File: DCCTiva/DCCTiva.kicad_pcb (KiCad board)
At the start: 2 copper layers, 50.8 x 34.3 mm, 11 parts, among them J1 TI_BOOSTER_40_J1, J2 TI_BOOSTER_40_J2, J3 TI_BOOSTER_40_J3, J4 TI_BOOSTER_40_J4, P1 Power and DCC, U1 LMD18200

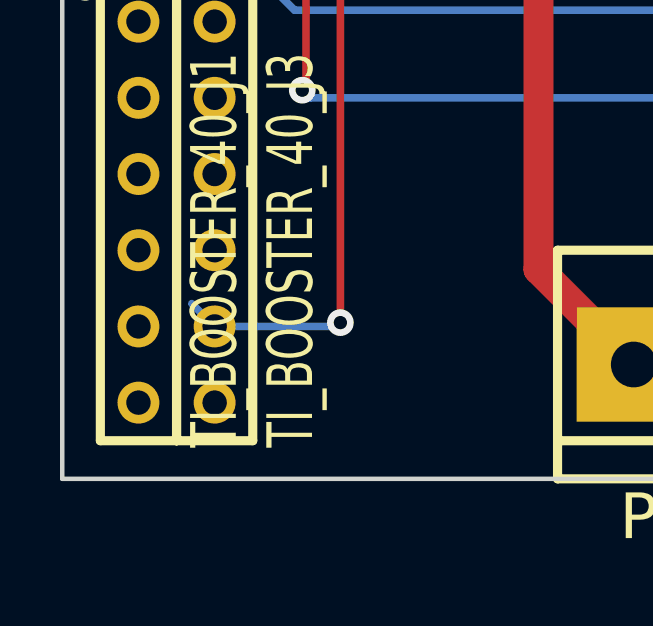
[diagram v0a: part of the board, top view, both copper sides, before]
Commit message: Add Current Sense line
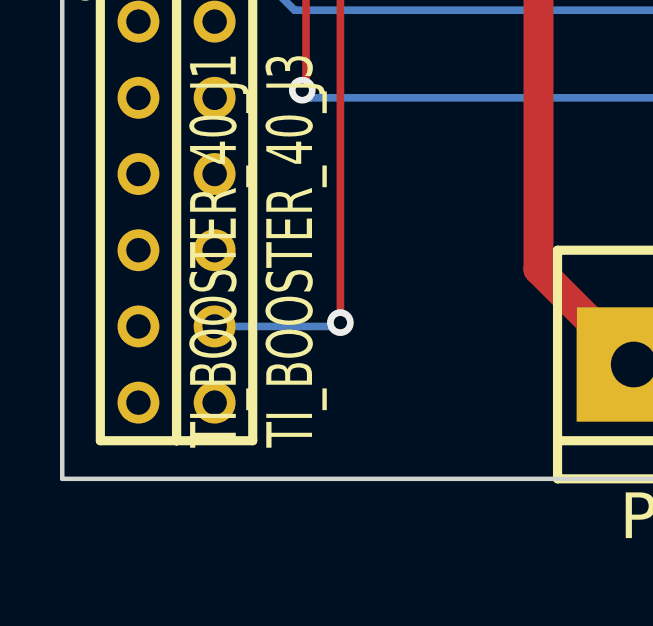
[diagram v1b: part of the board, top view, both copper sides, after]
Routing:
- net /Current Sense: track 48.1 -> 47.0 mm
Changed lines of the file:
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@@
     (thickness 1.6)
     (drawings 7)
-    (tracks 121)
+    (tracks 120)
     (zones 0)
     (modules 11)
@@
   (segment (start 192.532 129.54) (end 192.151 129.921) (width 0.254) (layer Front) (net 3))
   (via (at 192.532 129.54) (size 0.889) (layers Front Back) (net 3))
-  (segment (start 187.96 142.24) (end 187.198 141.478) (width 0.254) (layer Back) (net 3))
   (segment (start 200.66 129.54) (end 205.105 129.54) (width 0.254) (layer Back) (net 3))
   (segment (start 212.95 120.171) (end 212.95 118.59) (width 0.254) (layer Front) (net 3))

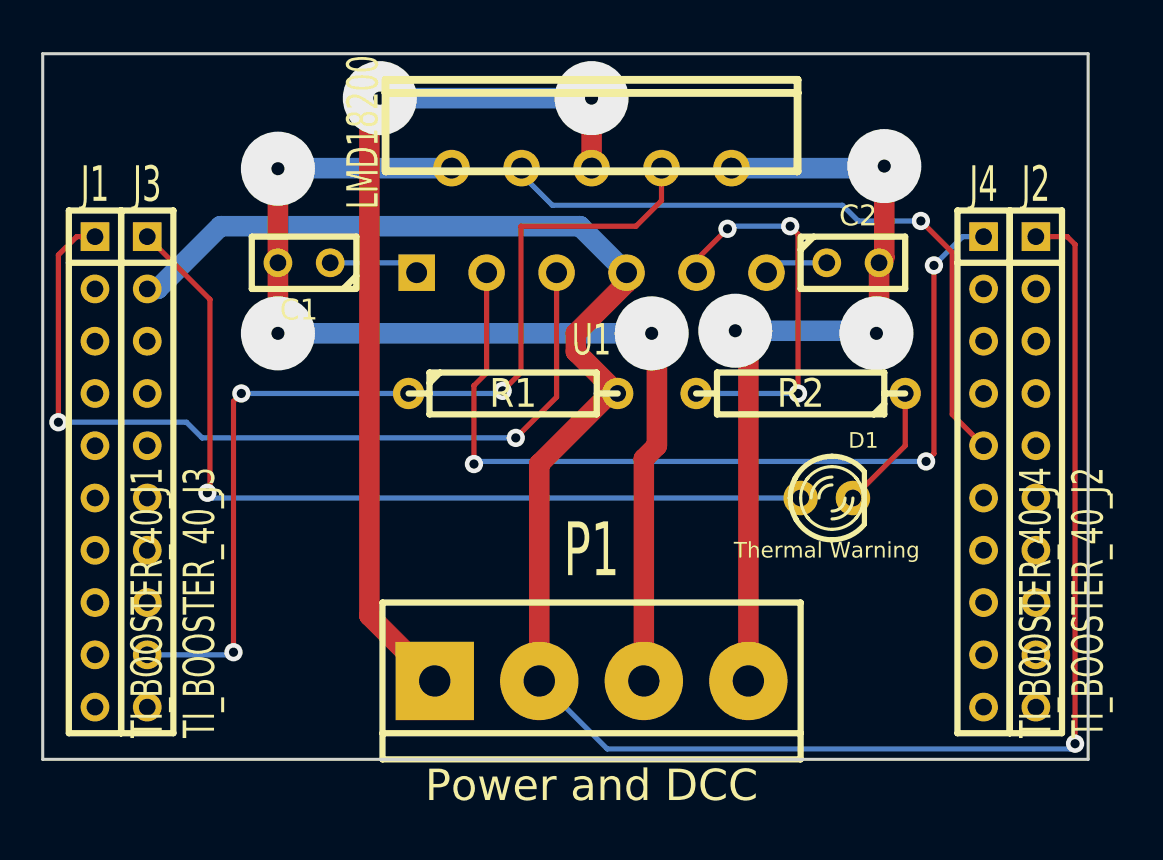
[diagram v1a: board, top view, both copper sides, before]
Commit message: Add support for I2C LCD.
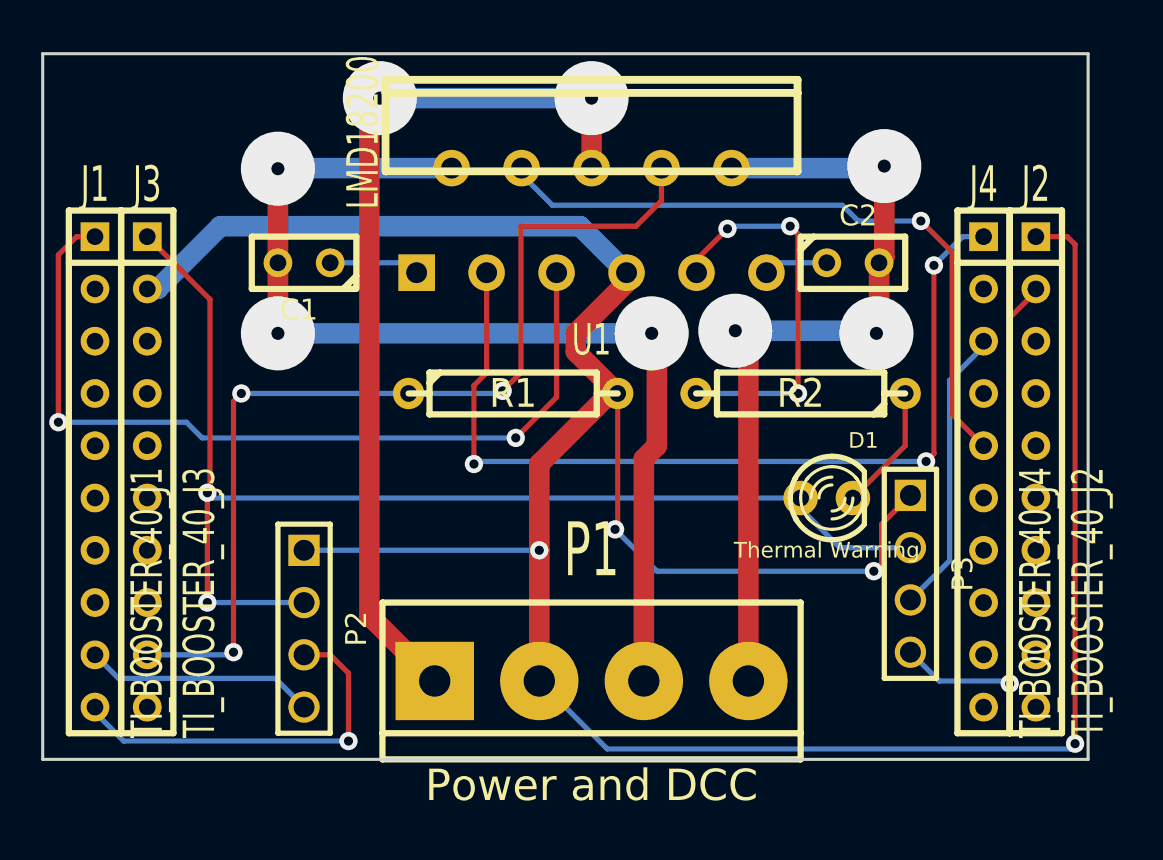
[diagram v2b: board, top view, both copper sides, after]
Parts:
- added P2: I2C 1, PIN_ARRAY_4x1, F.Cu at (195.6, 141.0)
- added P3: I2C 0, PIN_ARRAY_4x1, F.Cu at (225.0, 138.3)
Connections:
- J1 pad 10: (no net) -> /SDA - 1
- J1 pad 9: (no net) -> /SCL - 1
- J2 pad 2: (no net) -> /SCL - 0
- J4 pad 3: (no net) -> /SDA - 0
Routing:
- net GND: track 102.8 -> 138.7 mm, vias 1 -> 4
- net /SCL - 0: track 0.00 -> 25.3 mm, vias 0 -> 1
- net /SDA - 1: track 0.00 -> 19.0 mm, vias 0 -> 1
- net +5V: track 42.7 -> 59.4 mm, vias 1 -> 2
- net /SDA - 0: track 0.00 -> 14.0 mm
- net /SCL - 1: track 0.00 -> 11.2 mm
